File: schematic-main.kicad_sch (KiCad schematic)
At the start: 45 parts, among them J1 Conn_01x02_Socket, J2 Conn_01x04_Pin, J4 Conn_01x02_Pin, P1 USB_C_Plug_USB2.0, SW1 SW_Push, U1 STM32F042F6Px, U2 MQ-8, U3 SN65HVD232, U5 USBLC6-2P6, U6 ESP32-S3FN8, Y1 Crystal_GND24

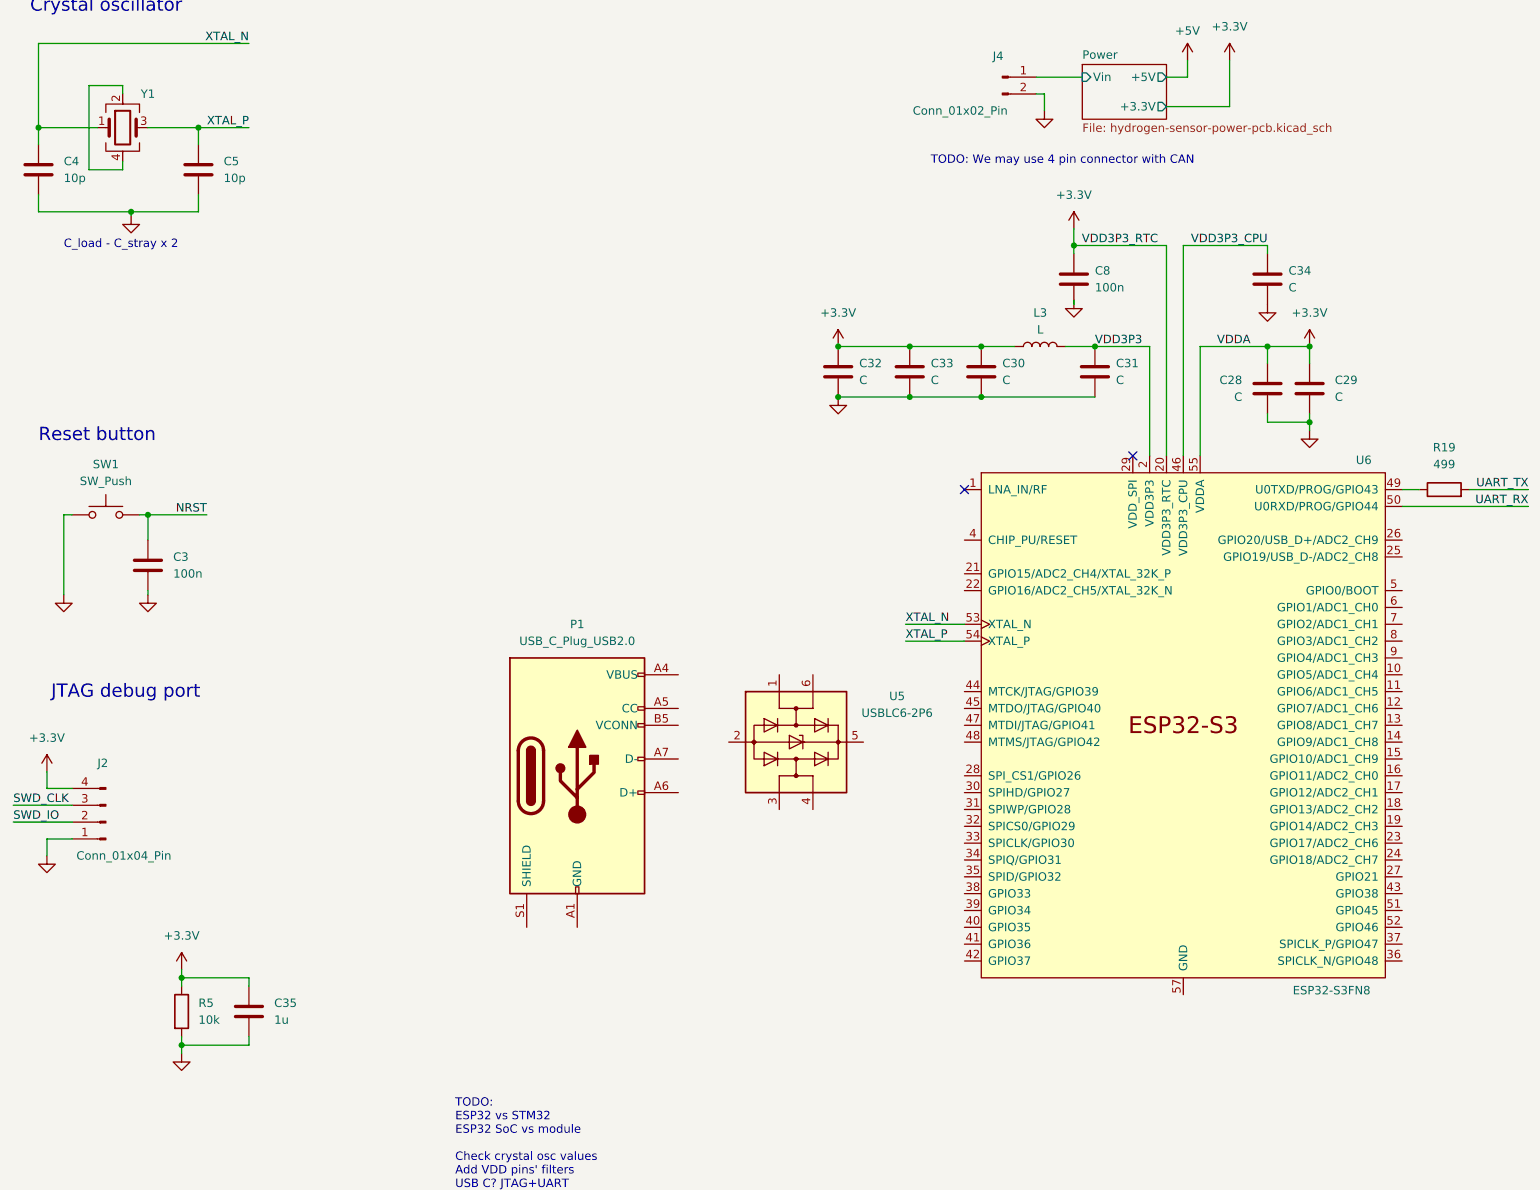
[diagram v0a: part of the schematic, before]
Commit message: Rename project files and setup crystal oscillator
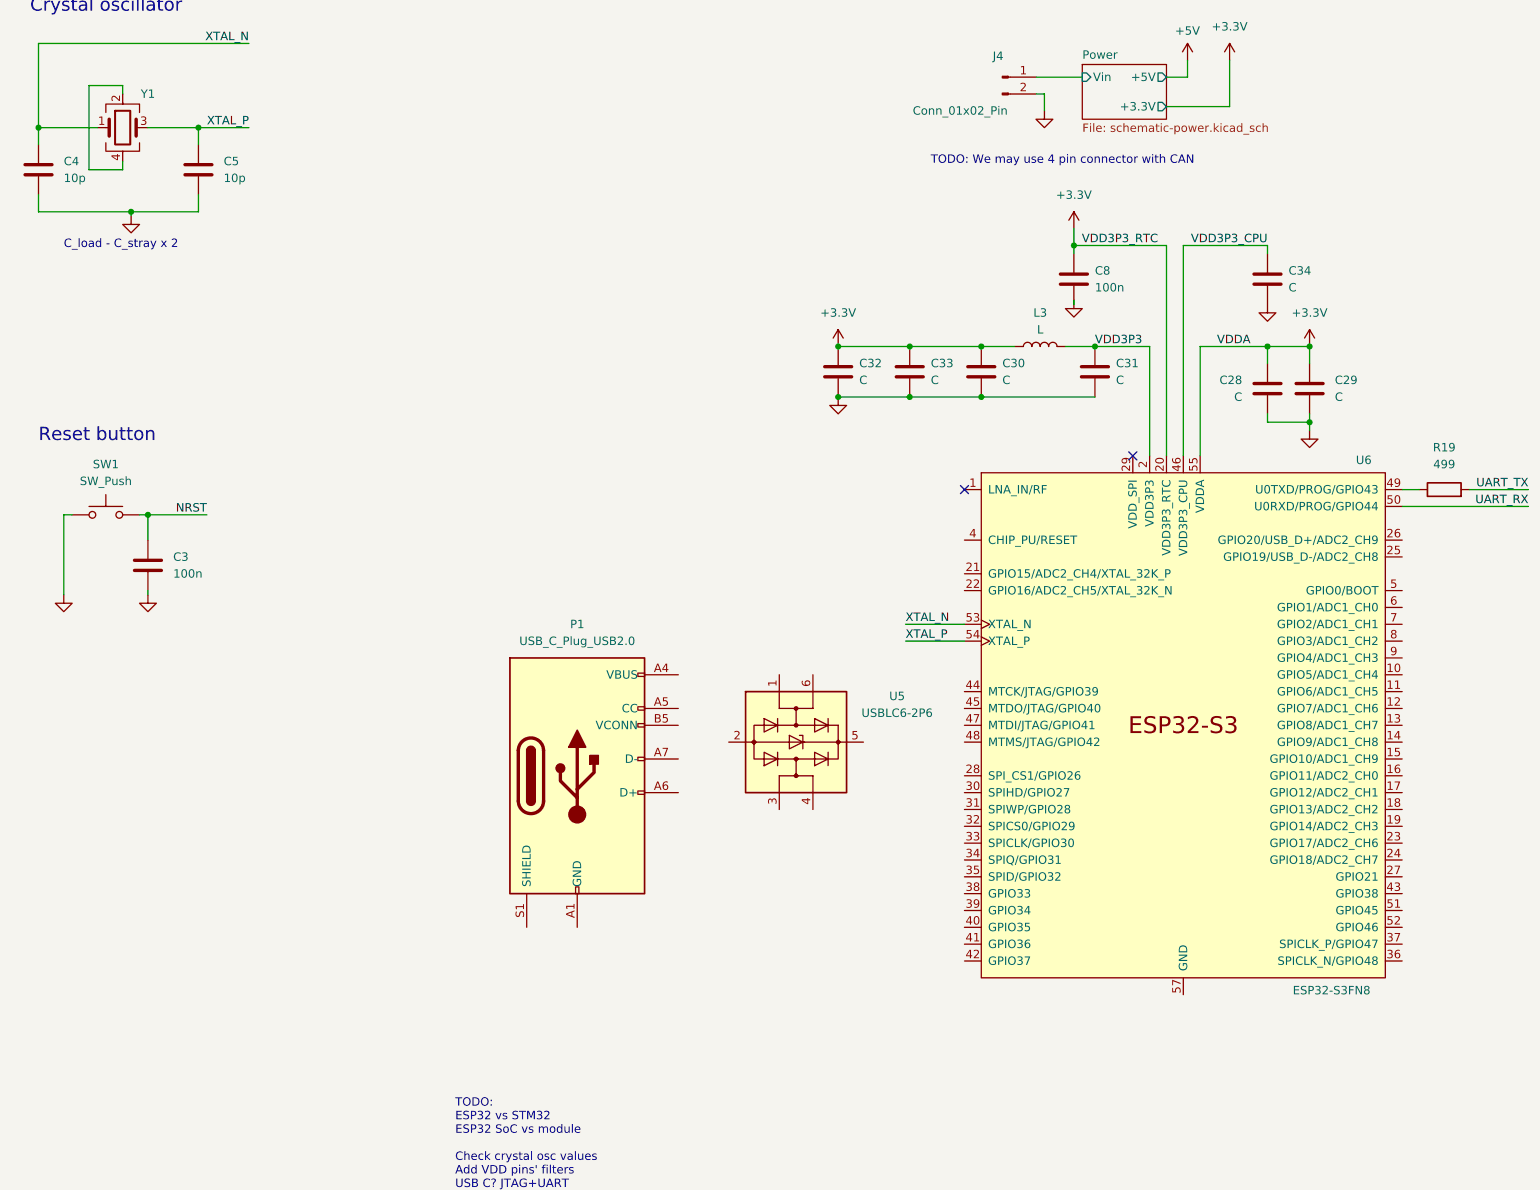
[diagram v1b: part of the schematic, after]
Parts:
- removed C35: 1u, symbol Device:C
- removed J2: Conn_01x04_Pin, symbol Connector:Conn_01x04_Pin
- removed R5: 10k, symbol Device:R
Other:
- sheet Power : file hydrogen-sensor-power-pcb.kicad_sch -> schematic-power.kicad_sch
- note removed: "JTAG debug port"

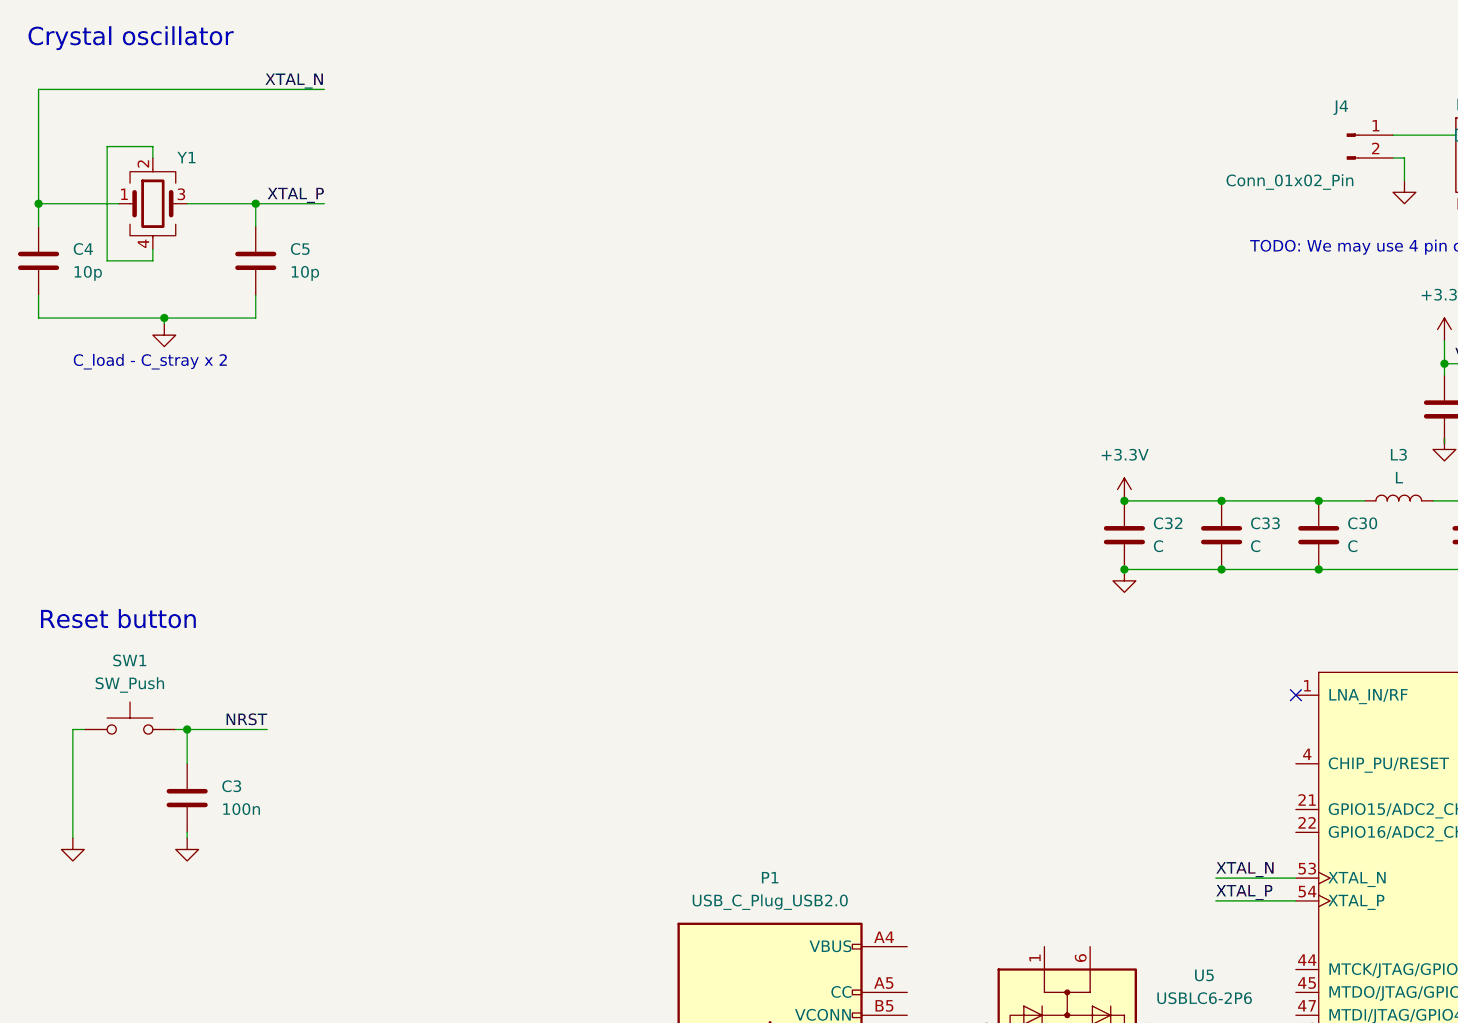
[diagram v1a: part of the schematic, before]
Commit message: Add reset button
Ground crystal oscillator shield
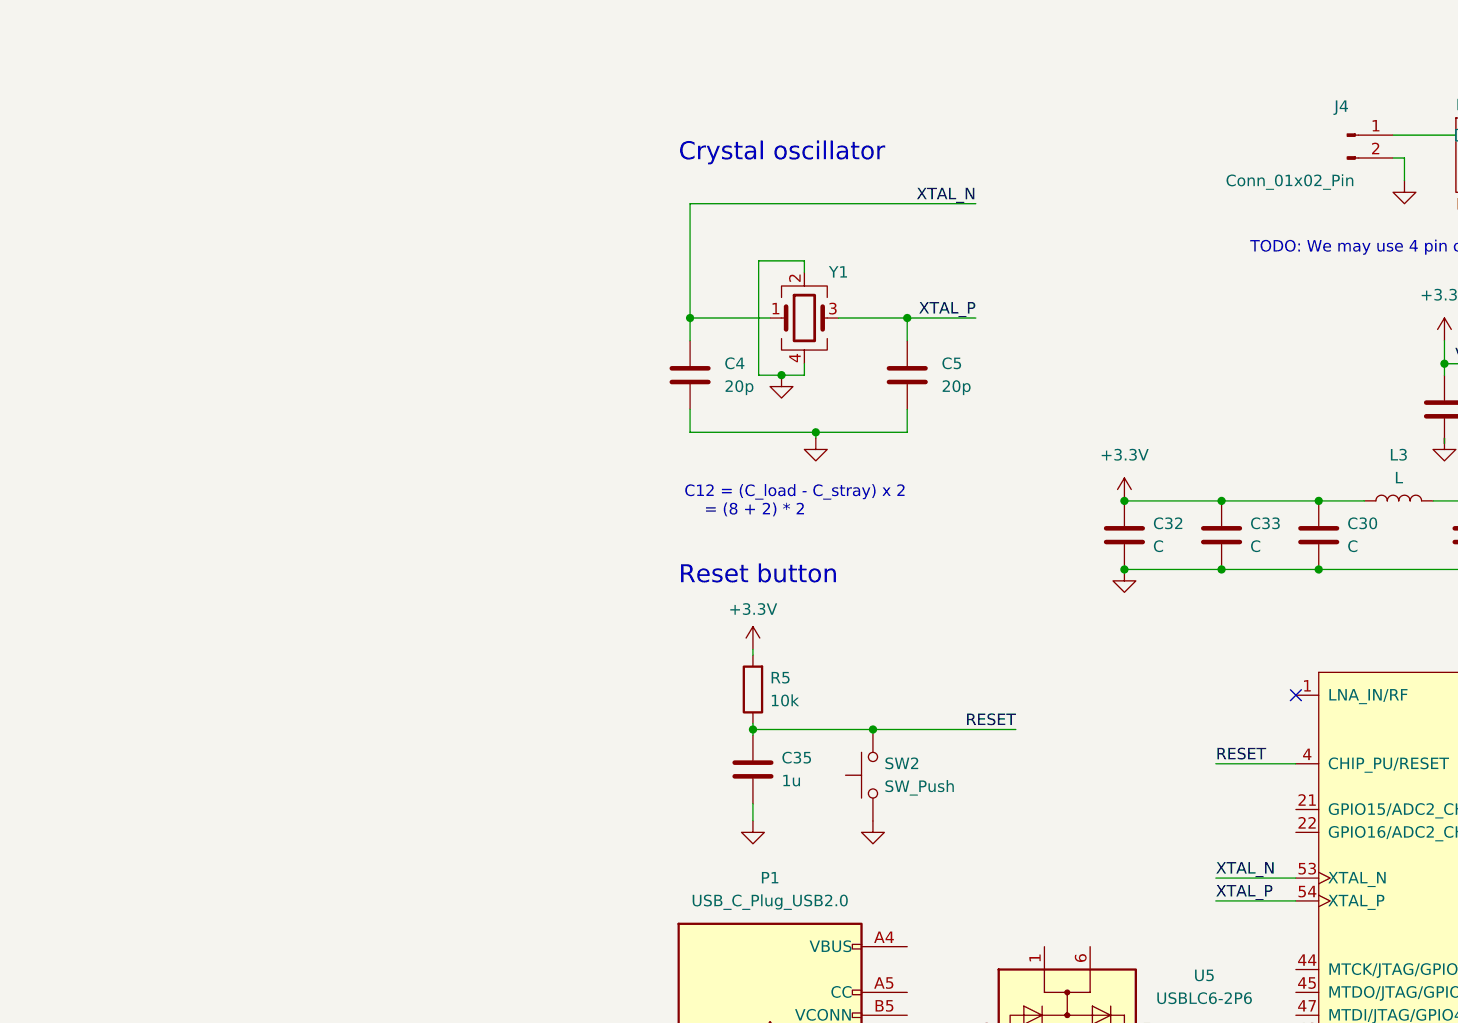
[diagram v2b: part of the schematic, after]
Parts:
- removed C3: 100n, symbol Device:C
- removed SW1: SW_Push, symbol Switch:SW_Push
- added C35: 1u, symbol Device:C
- added R5: 10k, symbol Device:R
- added SW2: SW_Push, symbol Switch:SW_Push
- C4, C5: value 10p -> 20p
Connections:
- net +3.3V: now also R5.2
- net GND: now also Y1.2, Y1.4, C35.2, SW2.1
- net RESET: now reaches U6.4 (CHIP_PU/RESET)
- net RESET: now also C35.1, R5.1, SW2.2
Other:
- note added: "C12 = (C_load - C_stray) x 2 = (8 + 2) * 2"
- note removed: "C_load - C_stray x 2"
- moved on the sheet: C4, C5, Y1

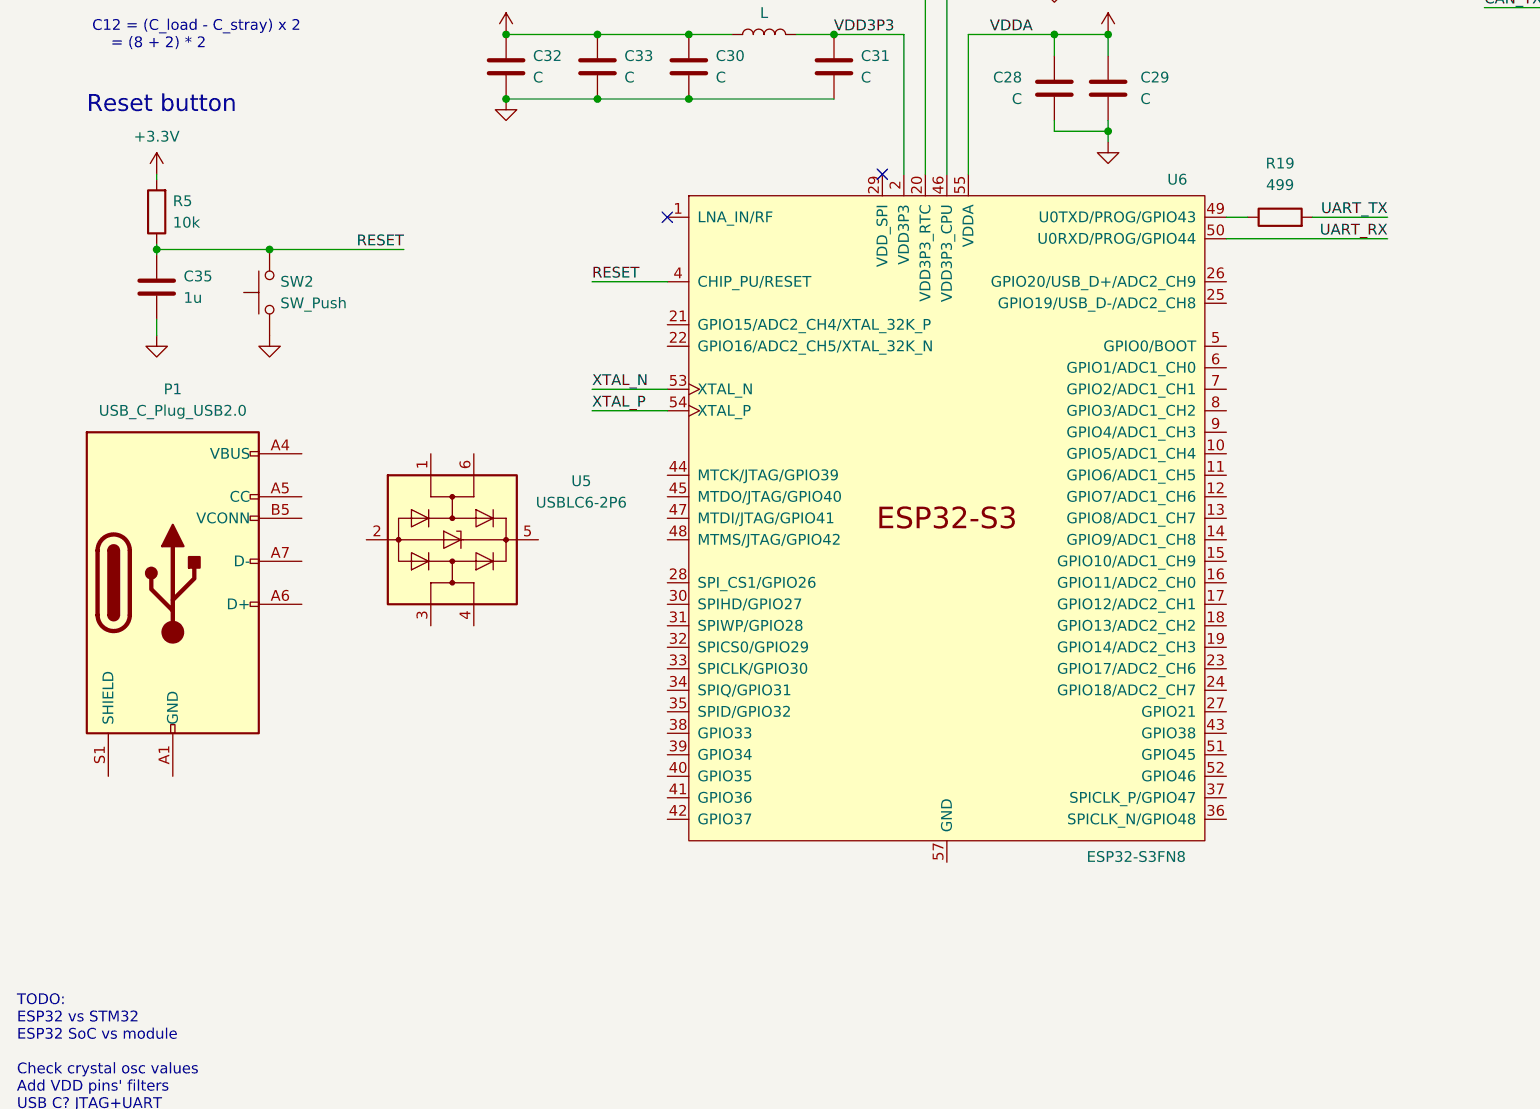
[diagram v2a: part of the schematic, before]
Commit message: Complete USB-C
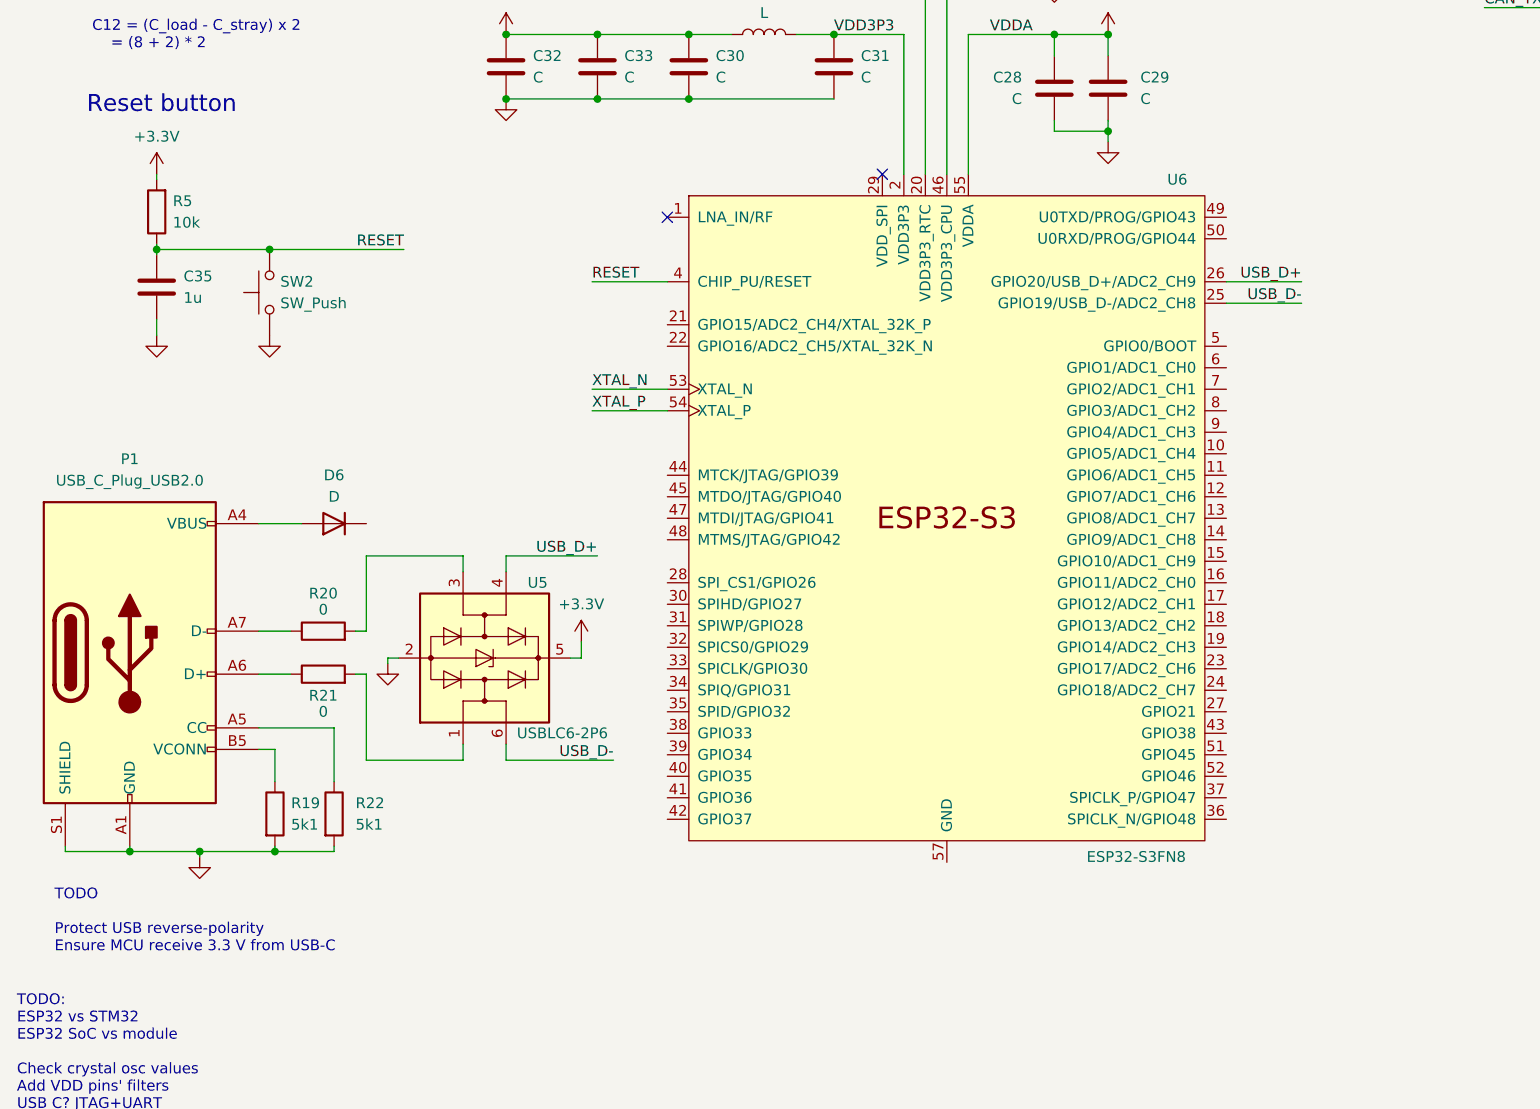
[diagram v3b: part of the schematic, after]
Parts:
- added D6: D, symbol Device:D
- added R20, R21: 0, symbol Device:R
- added R22: 5k1, symbol Device:R
- R19: value 499 -> 5k1
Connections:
- net UART_TX is gone; now on net GND: R19.2
- net +3.3V: now also U5.5 (VBUS)
- net GND: now also P1.A1 (GND), P1.A12 (GND), P1.B1 (GND), P1.B12 (GND), P1.S1 (SHIELD), U5.2 (GND), R22.2
- net USB_D-: now reaches U6.25 (GPIO19/USB_D-/ADC2_CH8)
- net USB_D-: now also U5.6 (I/O1)
- net USB_D+: now reaches U6.26 (GPIO20/USB_D+/ADC2_CH9)
- net USB_D+: now also U5.4 (I/O2)
- net at U6.49 (U0TXD/PROG/GPIO43): no longer R19.1
- net at U5.1 (I/O1): now also R21.2
- net at U5.3 (I/O2): now also R20.2
- net at P1.A4 (VBUS), P1.A9 (VBUS), P1.B4 (VBUS)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: now also D6.2 (A)
- net at P1.A5 (CC): now also R22.1
- net at P1.A6 (D+): now also R21.1
- net at P1.A7 (D-): now also R20.1
- net at P1.B5 (VCONN): now also R19.1
- net UART_RX: no longer names the net of U6.50 (U0RXD/PROG/GPIO44)
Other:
- note added: "TODO Protect USB reverse-polarity Ensure MCU receive 3.3 V from USB-C"
- moved on the sheet: P1, U5
